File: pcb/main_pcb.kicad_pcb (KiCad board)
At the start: 2 copper layers, 62 x 67 mm, 29 parts, among them J1 Conn_01x06_Socket, J2 Conn_01x10_Pin, J3 Conn_01x06_Pin, J4 USB_C_Receptacle_USB2.0, SW1 PAIR, SW2 RESET, SW3 BOOT, U1 ESP32-H2-MINI-1, U2 LM5165Y

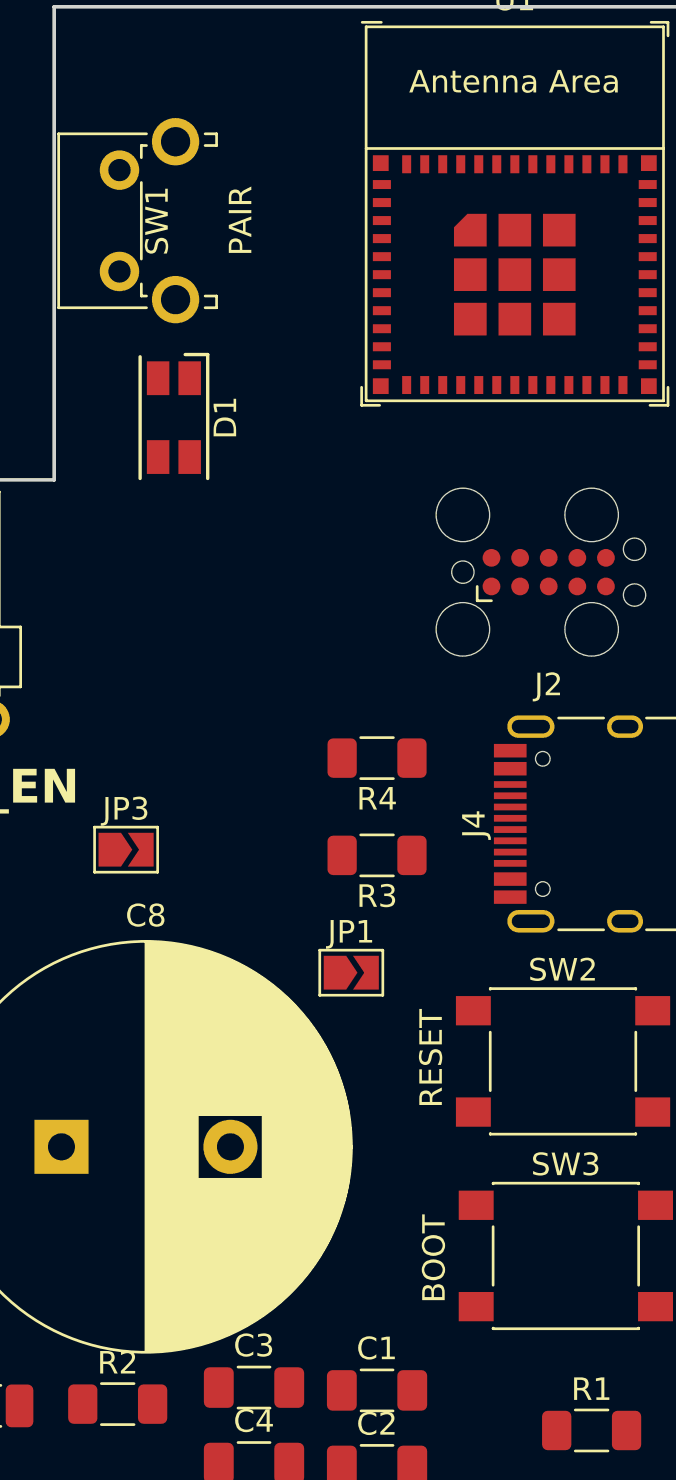
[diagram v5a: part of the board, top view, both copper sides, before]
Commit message: Add ESD protection to USB data lines
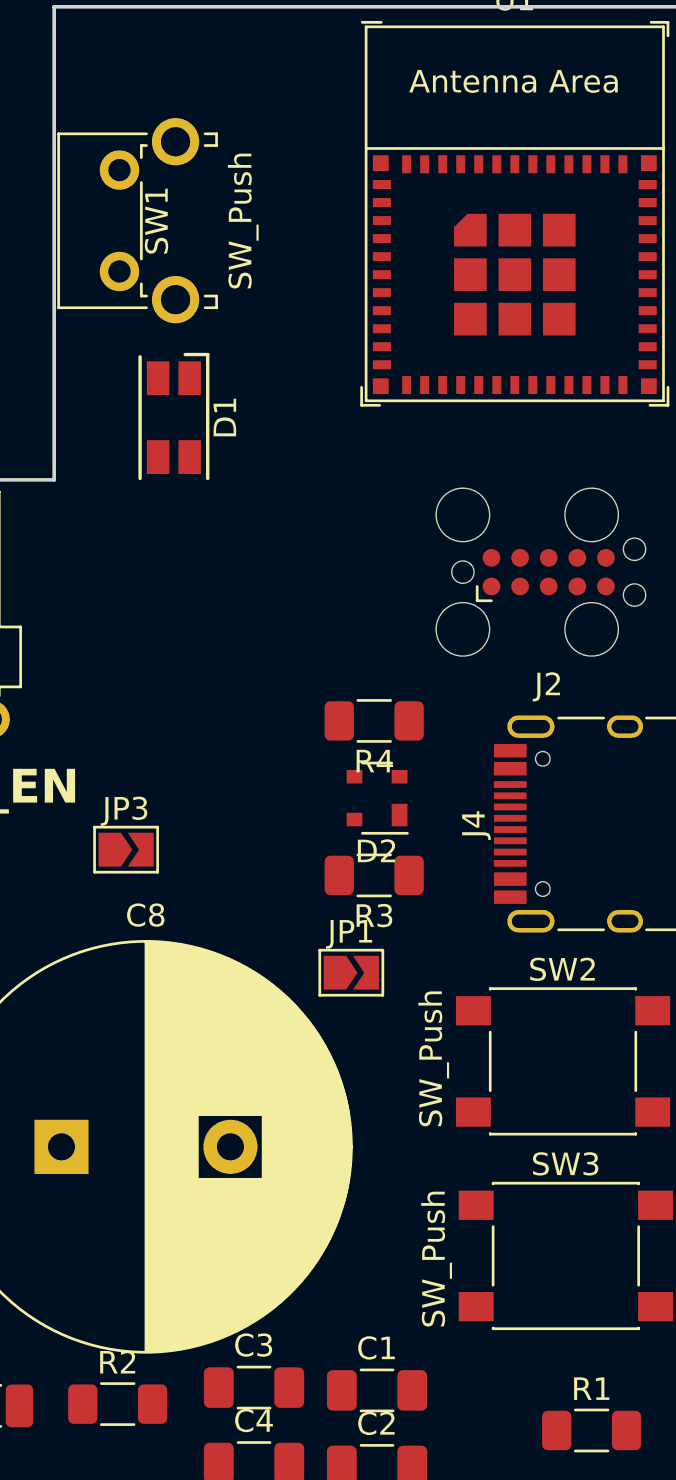
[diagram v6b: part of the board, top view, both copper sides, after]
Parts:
- added D2: SP0503BAHT, Package_TO_SOT_SMD:SOT-143, F.Cu at (156.8, 78.4)
- SW1: value PAIR -> SW_Push
- SW2: value RESET -> SW_Push
- SW3: value BOOT -> SW_Push
- moved R4 1.66 mm to (156.7, 74.9)
- moved R3 0.90 mm to (156.7, 81.8)
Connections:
- net Net-(JP3-A) renamed VBUS
- R6 pad 1: Net-(U1-GPIO12) -> Net-(U1-GPIO9)
- U1 pad 16: Net-(U1-GPIO12) -> unconnected-(U1-GPIO12-Pad16)
- U1 pad 23: unconnected-(U1-GPIO9-Pad23) -> Net-(U1-GPIO9)
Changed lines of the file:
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@@
   (net 12 "unconnected-(U1-GPIO10{slash}ZCD0-Pad20)")
   (net 13 "unconnected-(U1-GPIO11{slash}ZCD1-Pad21)")
-  (net 14 "unconnected-(U1-GPIO9-Pad23)")
+  (net 14 "VBUS")
   (net 15 "unconnected-(U1-GPIO22-Pad24)")
   (net 16 "unconnected-(U1-GPIO25{slash}FSPICS3-Pad25)")
-  (net 17 "Net-(JP3-A)")
+  (net 17 "Net-(U1-GPIO9)")
   (net 18 "Net-(J4-CC1)")
   (net 19 "unconnected-(U1-NC-Pad28)")
@@
   (net 57 "unconnected-(J4-SHIELD-PadS1)")
   (net 58 "Net-(U1-GPIO8)")
-  (net 59 "Net-(U1-GPIO12)")
+  (net 59 "unconnected-(U1-GPIO12-Pad16)")
   (net 60 "Net-(R6-Pad2)")
   (footprint "Button_Switch_SMD:SW_SPST_PTS645" (layer "F.Cu")
@@
         (effects (font (size 1 1) (thickness 0.15)))
     )
-    (fp_text value "BOOT" (at -5.842 0.127 90) (layer "F.SilkS")
+    (fp_text value "SW_Push" (at -5.842 0.127 90) (layer "F.SilkS")
         (effects (font (size 1 1) (thickness 0.15)))
     )
@@
         (effects (font (size 1 1) (thickness 0.15)))
     )
-    (fp_text value "PAIR" (at 2.25 5.38988 90) (layer "F.SilkS")
+    (fp_text value "SW_Push" (at 2.25 5.38988 90) (layer "F.SilkS")
         (effects (font (size 1 1) (thickness 0.15)))
     )
@@
       (stroke (width 0.05) (type solid)) (layer "F.CrtYd"))
     (pad "1" smd custom (at -0.725 0) (size 0.3 0.3) (layers "F.Cu" "F.Mask")
-      (net 17 "Net-(JP3-A)") (pinfunction "A") (pintype "passive") (zone_connect 2)
+      (net 14 "VBUS") (pinfunction "A") (pintype "passive") (zone_connect 2)
       (options (clearance outline) (anchor rect))
       (primitives
@@
       (net 32 "GND") (pinfunction "GND") (pintype "passive"))
     (pad "A4" smd rect (at -2.45 -4.045 90) (size 0.6 1.45) (layers "F.Cu" "F.Paste" "F.Mask")
-      (net 17 "Net-(JP3-A)") (pinfunction "VBUS") (pintype "passive"))
+      (net 14 "VBUS") (pinfunction "VBUS") (pintype "passive"))
     (pad "A5" smd rect (at -1.25 -4.045 90) (size 0.3 1.45) (layers "F.Cu" "F.Paste" "F.Mask")
       (net 18 "Net-(J4-CC1)") (pinfunction "CC1") (pintype "bidirectional"))
@@
       (net 54 "unconnected-(J4-SBU1-PadA8)") (pinfunction "SBU1") (pintype "bidirectional+no_connect"))
     (pad "A9" smd rect (at 2.45 -4.045 90) (size 0.6 1.45) (layers "F.Cu" "F.Paste" "F.Mask")
-      (net 17 "Net-(JP3-A)") (pinfunction "VBUS") (pintype "passive"))
+      (net 14 "VBUS") (pinfunction "VBUS") (pintype "passive"))
     (pad "A12" smd rect (at 3.25 -4.045 90) (size 0.6 1.45) (layers "F.Cu" "F.Paste" "F.Mask")
       (net 32 "GND") (pinfunction "GND") (pintype "passive"))
@@
       (net 32 "GND") (pinfunction "GND") (pintype "passive"))
     (pad "B4" smd rect (at 2.45 -4.045 90) (size 0.6 1.45) (layers "F.Cu" "F.Paste" "F.Mask")
-      (net 17 "Net-(JP3-A)") (pinfunction "VBUS") (pintype "passive"))
+      (net 14 "VBUS") (pinfunction "VBUS") (pintype "passive"))
     (pad "B5" smd rect (at 1.75 -4.045 90) (size 0.3 1.45) (layers "F.Cu" "F.Paste" "F.Mask")
       (net 55 "Net-(J4-CC2)") (pinfunction "CC2") (pintype "bidirectional"))
@@
       (net 56 "unconnected-(J4-SBU2-PadB8)") (pinfunction "SBU2") (pintype "bidirectional+no_connect"))
     (pad "B9" smd rect (at -2.45 -4.045 90) (size 0.6 1.45) (layers "F.Cu" "F.Paste" "F.Mask")
-      (net 17 "Net-(JP3-A)") (pinfunction "VBUS") (pintype "passive"))
+      (net 14 "VBUS") (pinfunction "VBUS") (pintype "passive"))
     (pad "B12" smd rect (at -3.25 -4.045 90) (size 0.6 1.45) (layers "F.Cu" "F.Paste" "F.Mask")
       (net 32 "GND") (pinfunction "GND") (pintype "passive"))
@@
       (stroke (width 0.1) (type solid)) (layer "F.Fab"))
     (pad "1" smd roundrect (at -1.55 0) (size 1.3 1.75) (layers "F.Cu" "F.Paste" "F.Mask") (roundrect_rratio 0.192308)
-      (net 59 "Net-(U1-GPIO12)") (pintype "passive"))
+      (net 17 "Net-(U1-GPIO9)") (pintype "passive"))
     (pad "2" smd roundrect (at 1.55 0) (size 1.3 1.75) (layers "F.Cu" "F.Paste" "F.Mask") (roundrect_rratio 0.192308)
       (net 60 "Net-(R6-Pad2)") (pintype "passive"))
@@
       (net 10 "unconnected-(U1-VBAT-Pad15)") (pinfunction "VBAT") (pintype "input"))
     (pad "16" smd rect (at -1.6 7.6) (size 0.4 0.8) (layers "F.Cu" "F.Paste" "F.Mask")
-      (net 59 "Net-(U1-GPIO12)") (pinfunction "GPIO12") (pintype "bidirectional"))
+      (net 59 "unconnected-(U1-GPIO12-Pad16)") (pinfunction "GPIO12") (pintype "bidirectional"))
     (pad "17" smd rect (at -0.8 7.6) (size 0.4 0.8) (layers "F.Cu" "F.Paste" "F.Mask")
       (net 11 "unconnected-(U1-NC-Pad17)") (pinfunction "NC") (pintype "no_connect"))
@@
       (net 58 "Net-(U1-GPIO8)") (pinfunction "GPIO8") (pintype "bidirectional"))
     (pad "23" smd rect (at 4 7.6) (size 0.4 0.8) (layers "F.Cu" "F.Paste" "F.Mask")
-      (net 14 "unconnected-(U1-GPIO9-Pad23)") (pinfunction "GPIO9") (pintype "bidirectional"))
+      (net 17 "Net-(U1-GPIO9)") (pinfunction "GPIO9") (pintype "bidirectional"))
     (pad "24" smd rect (at 4.8 7.6) (size 0.4 0.8) (layers "F.Cu" "F.Paste" "F.Mask")
       (net 15 "unconnected-(U1-GPIO22-Pad24)") (pinfunction "GPIO22") (pintype "bidirectional"))
@@
     )
   )
+  (footprint "Package_TO_SOT_SMD:SOT-143" (layer "F.Cu")
+    (at 156.845 78.359 180)
+    (descr "SOT-143 https://www.nxp.com/docs/en/package-information/SOT143B.pdf")
+    (tags "SOT-143")
+    (property "Sheetfile" "main_pcb.kicad_sch")
+    (property "Sheetname" "")
+    (property "ki_description" "TVS Diode Array, 5.5V Standoff, 3 Channels, SOT-143 package")
+    (property "ki_keywords" "usb esd protection suppression transient")
+    (attr smd)
+    (fp_text reference "D2" (at 0.02 -2.38) (layer "F.SilkS")
+        (effects (font (size 1 1) (thickness 0.15)))
+    )
+    (fp_text value "SP0503BAHT" (at -0.28 2.48) (layer "F.Fab")
+        (effects (font (size 1 1) (thickness 0.15)))
+    )
+    (fp_text user "${REFERENCE}" (at 0 0 90) (layer "F.Fab")
+        (effects (font (size 0.5 0.5) (thickness 0.075)))
+    )
+    (fp_line (start -0.65 1.56) (end 0.65 1.56)
+      (stroke (width 0.12) (type solid)) (layer "F.SilkS"))
+    (fp_line (start 0.65 -1.56) (end -1.35 -1.56)
+      (stroke (width 0.12) (type solid)) (layer "F.SilkS"))
+    (fp_line (start -1.6 1.7) (end -1.6 -1.7)
+      (stroke (width 0.05) (type solid)) (layer "F.CrtYd"))
+    (fp_line (start -1.6 1.7) (end 1.6 1.7)
+      (stroke (width 0.05) (type solid)) (layer "F.CrtYd"))
+    (fp_line (start 1.6 -1.7) (end -1.6 -1.7)
+      (stroke (width 0.05) (type solid)) (layer "F.CrtYd"))
+    (fp_line (start 1.6 -1.7) (end 1.6 1.7)
+      (stroke (width 0.05) (type solid)) (layer "F.CrtYd"))
+    (fp_line (start -0.65 -0.95) (end -0.15 -1.45)
+      (stroke (width 0.1) (type solid)) (layer "F.Fab"))
+    (fp_line (start -0.65 1.45) (end -0.65 -0.95)
+      (stroke (width 0.1) (type solid)) (layer "F.Fab"))
+    (fp_line (start -0.15 -1.45) (end 0.65 -1.45)
+      (stroke (width 0.1) (type solid)) (layer "F.Fab"))
+    (fp_line (start 0.65 -1.45) (end 0.65 1.45)
+      (stroke (width 0.1) (type solid)) (layer "F.Fab"))
+    (fp_line (start 0.65 1.45) (end -0.65 1.45)
+      (stroke (width 0.1) (type solid)) (layer "F.Fab"))
+    (pad "1" smd rect (at -1 -0.75 180) (size 0.7 1) (layers "F.Cu" "F.Paste" "F.Mask")
+      (net 32 "GND") (pinfunction "A") (pintype "passive"))
+    (pad "2" smd rect (at -1 0.95 180) (size 0.7 0.6) (layers "F.Cu" "F.Paste" "F.Mask")
+      (net 52 "/D+") (pinfunction "K") (pintype "passive"))
+    (pad "3" smd rect (at 1 0.95 180) (size 0.7 0.6) (layers "F.Cu" "F.Paste" "F.Mask")
+      (net 53 "/D-") (pinfunction "K") (pintype "passive"))
+    (pad "4" smd rect (at 1 -0.95 180) (size 0.7 0.6) (layers "F.Cu" "F.Paste" "F.Mask")
+      (net 14 "VBUS") (pinfunction "K") (pintype "passive"))
+    (model "${KICAD6_3DMODEL_DIR}/Package_TO_SOT_SMD.3dshapes/SOT-143.wrl"
+      (offset (xyz 0 0 0))
+      (scale (xyz 1 1 1))
+      (rotate (xyz 0 0 0))
+    )
+  )
   (footprint "Connector_PinHeader_2.54mm:PinHeader_1x06_P2.54mm_Horizontal" (layer "F.Cu")
     (at 120.65 74.86 90)
@@
   )
   (footprint "Resistor_SMD:R_1206_3216Metric_Pad1.30x1.75mm_HandSolder" (layer "F.Cu")
-    (at 156.845 76.581 180)
+    (at 156.718 74.93 180)
     (descr "Resistor SMD 1206 (3216 Metric), square (rectangular) end terminal, IPC_7351 nominal with elongated pad for handsoldering. (Body size source: IPC-SM-782 page 72, https://www.pcb-3d.com/wordpress/wp-content/uploads/ipc-sm-782a_amendment_1_and_2.pdf), generated with kicad-footprint-generator")
     (tags "resistor handsolder")
@@
         (effects (font (size 1 1) (thickness 0.15)))
     )
-    (fp_text user "${REFERENCE}" (at 0 0) (layer "F.Fab")
+    (fp_text user "${REFERENCE}" (at 0 0.8) (layer "F.Fab")
         (effects (font (size 0.8 0.8) (thickness 0.12)))
     )
@@
   )
   (footprint "Resistor_SMD:R_1206_3216Metric_Pad1.30x1.75mm_HandSolder" (layer "F.Cu")
-    (at 156.845 80.899 180)
+    (at 156.718 81.788 180)
     (descr "Resistor SMD 1206 (3216 Metric), square (rectangular) end terminal, IPC_7351 nominal with elongated pad for handsoldering. (Body size source: IPC-SM-782 page 72, https://www.pcb-3d.com/wordpress/wp-content/uploads/ipc-sm-782a_amendment_1_and_2.pdf), generated with kicad-footprint-generator")
     (tags "resistor handsolder")
@@
         (effects (font (size 1 1) (thickness 0.15)))
     )
-    (fp_text value "RESET" (at -5.842 -0.127 270) (layer "F.SilkS")
-        (effects (font (size 1 1) (thickness 0.15)))
-    )
+    (fp_text value "SW_Push" (at -5.842 -0.127 270) (layer "F.SilkS")
+        (effects (font (size 1 1) (thickness 0.15)))
+    )
